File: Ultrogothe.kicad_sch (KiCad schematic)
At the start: 2 parts, among them J1 Conn_01x20, J2 Conn_01x20

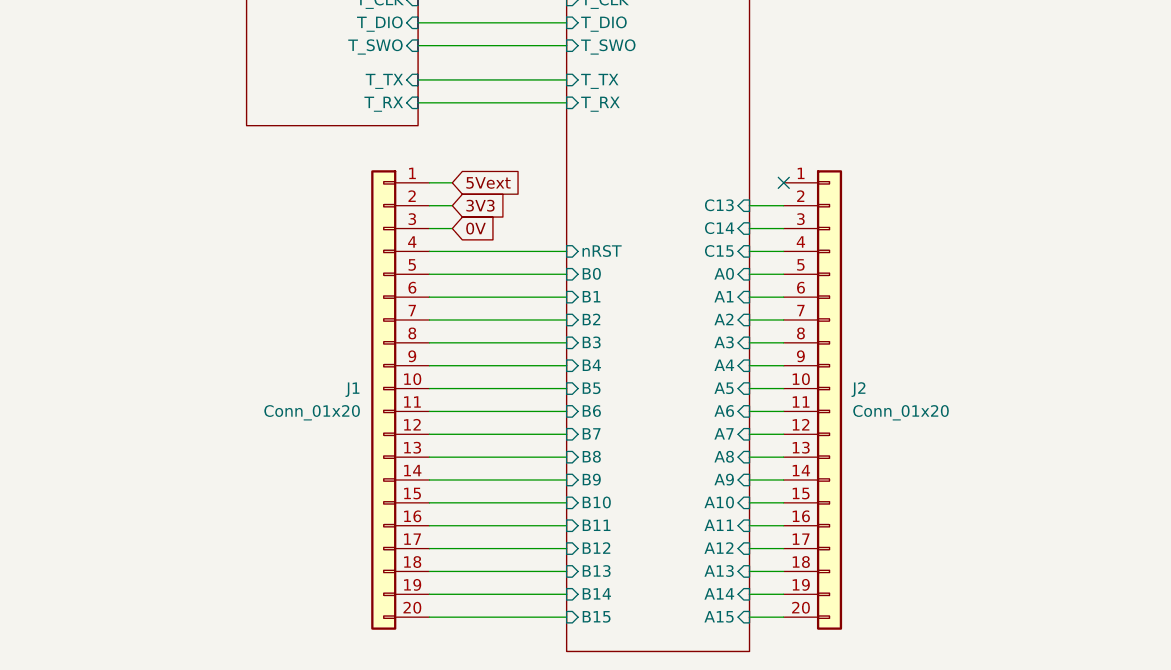
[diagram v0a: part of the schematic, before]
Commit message: répartition pins encours
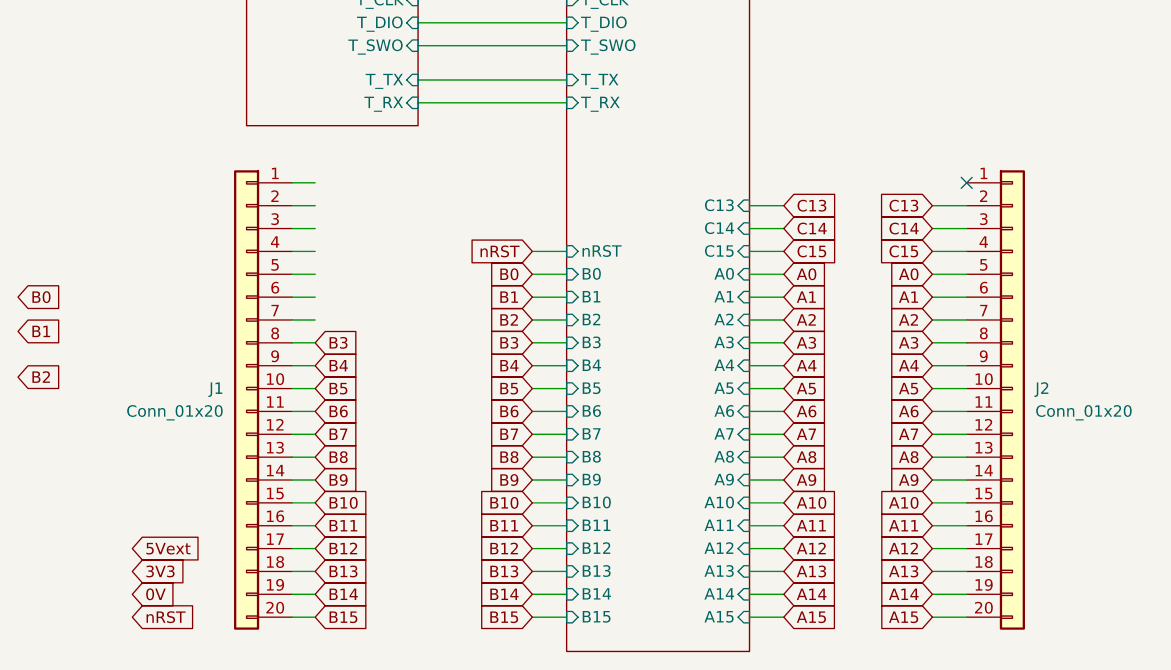
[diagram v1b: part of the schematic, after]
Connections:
- net 0V: no longer J1.3 (Pin_3)
- net 3V3: no longer J1.2 (Pin_2)
- net 5Vext: no longer J1.1 (Pin_1)
- net s_uC/A0 renamed A0
- net s_uC/A1 renamed A1
- net s_uC/A10 renamed A10
- net s_uC/A11 renamed A11
- net s_uC/A12 renamed A12
- net s_uC/A13 renamed A13
- net s_uC/A14 renamed A14
- net s_uC/A15 renamed A15
- net s_uC/A2 renamed A2
- net s_uC/A3 renamed A3
- net s_uC/A4 renamed A4
- net s_uC/A5 renamed A5
- net s_uC/A6 renamed A6
- net s_uC/A7 renamed A7
- net s_uC/A8 renamed A8
- net s_uC/A9 renamed A9
- net s_uC/B0: no longer names the net of J1.5 (Pin_5)
- net s_uC/B1: no longer names the net of J1.6 (Pin_6)
- net s_uC/B10 renamed B10
- net s_uC/B11 renamed B11
- net s_uC/B12 renamed B12
- net s_uC/B13 renamed B13
- net s_uC/B14 renamed B14
- net s_uC/B15 renamed B15
- net s_uC/B2: no longer names the net of J1.7 (Pin_7)
- net s_uC/B3 renamed B3
- net s_uC/B4 renamed B4
- net s_uC/B5 renamed B5
- net s_uC/B6 renamed B6
- net s_uC/B7 renamed B7
- net s_uC/B8 renamed B8
- net s_uC/B9 renamed B9
- net s_uC/C13 renamed C13
- net s_uC/C14 renamed C14
- net s_uC/C15 renamed C15
- net s_uC/nRST: no longer names the net of J1.4 (Pin_4)
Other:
- moved on the sheet: J1, J2

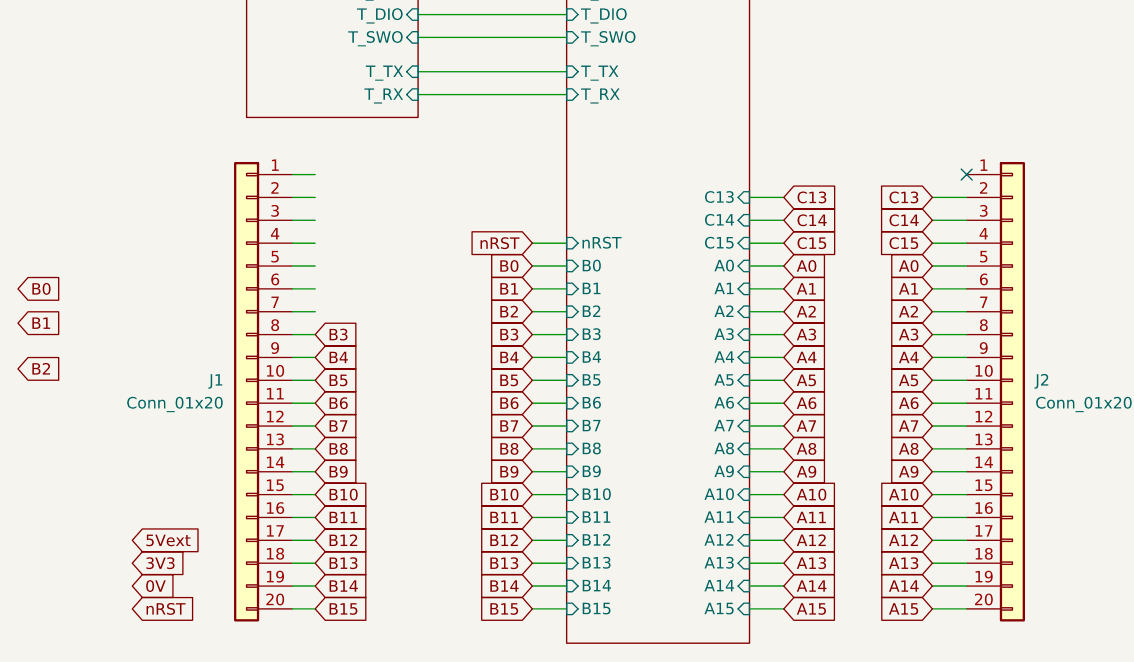
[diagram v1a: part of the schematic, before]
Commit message: répartition pins et routage
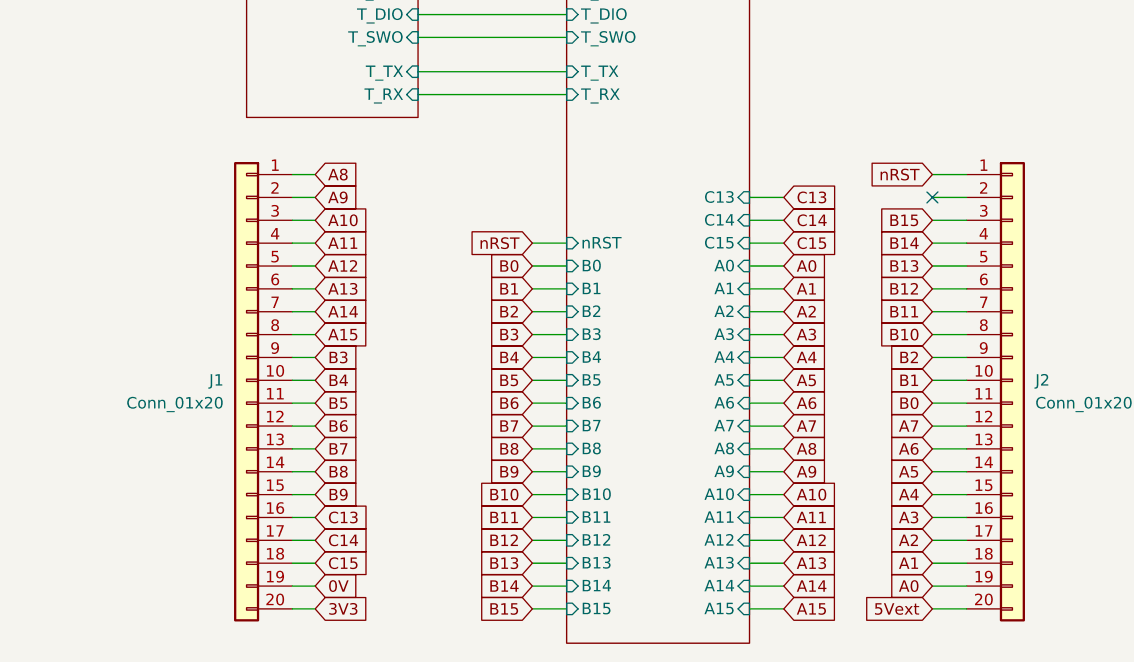
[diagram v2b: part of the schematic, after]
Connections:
- net 0V: now also J1.19 (Pin_19)
- net 3V3: now also J1.20 (Pin_20)
- net 5Vext: now also J2.20 (Pin_20)
- net A0: now also J2.19 (Pin_19); no longer J2.5 (Pin_5)
- net A1: now also J2.18 (Pin_18); no longer J2.6 (Pin_6)
- net A10: now also J1.3 (Pin_3); no longer J2.15 (Pin_15)
- net A11: now also J1.4 (Pin_4); no longer J2.16 (Pin_16)
- net A12: now also J1.5 (Pin_5); no longer J2.17 (Pin_17)
- net A13: now also J1.6 (Pin_6); no longer J2.18 (Pin_18)
- net A14: now also J1.7 (Pin_7); no longer J2.19 (Pin_19)
- net A15: now also J1.8 (Pin_8); no longer J2.20 (Pin_20)
- net A2: now also J2.17 (Pin_17); no longer J2.7 (Pin_7)
- net A3: now also J2.16 (Pin_16); no longer J2.8 (Pin_8)
- net A4: now also J2.15 (Pin_15); no longer J2.9 (Pin_9)
- net A5: now also J2.14 (Pin_14); no longer J2.10 (Pin_10)
- net A6: now also J2.13 (Pin_13); no longer J2.11 (Pin_11)
- net A8: now also J1.1 (Pin_1); no longer J2.13 (Pin_13)
- net A9: now also J1.2 (Pin_2); no longer J2.14 (Pin_14)
- net B0: now also J2.11 (Pin_11)
- net B1: now also J2.10 (Pin_10)
- net B10: now also J2.8 (Pin_8); no longer J1.15 (Pin_15)
- net B11: now also J2.7 (Pin_7); no longer J1.16 (Pin_16)
- net B12: now also J2.6 (Pin_6); no longer J1.17 (Pin_17)
- net B13: now also J2.5 (Pin_5); no longer J1.18 (Pin_18)
- net B14: now also J2.4 (Pin_4); no longer J1.19 (Pin_19)
- net B15: now also J2.3 (Pin_3); no longer J1.20 (Pin_20)
- net B2: now also J2.9 (Pin_9)
- net B3: now also J1.9 (Pin_9); no longer J1.8 (Pin_8)
- net B4: now also J1.10 (Pin_10); no longer J1.9 (Pin_9)
- net B5: now also J1.11 (Pin_11); no longer J1.10 (Pin_10)
- net B6: now also J1.12 (Pin_12); no longer J1.11 (Pin_11)
- net B7: now also J1.13 (Pin_13); no longer J1.12 (Pin_12)
- net B8: now also J1.14 (Pin_14); no longer J1.13 (Pin_13)
- net B9: now also J1.15 (Pin_15); no longer J1.14 (Pin_14)
- net C13: now also J1.16 (Pin_16); no longer J2.2 (Pin_2)
- net C14: now also J1.17 (Pin_17); no longer J2.3 (Pin_3)
- net C15: now also J1.18 (Pin_18); no longer J2.4 (Pin_4)
- net nRST: now also J2.1 (Pin_1)

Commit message: routage fini
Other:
- sheet s_debugger ports: added none; removed T_CLK, T_DIO, T_RST, T_RX, T_SWO, T_TX
- sheet s_uC ports: added none; removed T_CLK, T_DIO, T_RST, T_RX, T_SWO, T_TX
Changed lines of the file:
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@@
-    (stroke (width 0) (type default))
-  )
-  (wire (pts (xy 121.92 76.2) (xy 138.43 76.2))
-    (stroke (width 0) (type default))
-  )
-  (wire (pts (xy 121.92 73.66) (xy 138.43 73.66))
     (stroke (width 0) (type default))
   )
@@
     (stroke (width 0) (type default))
   )
-  (wire (pts (xy 121.92 71.12) (xy 138.43 71.12))
-    (stroke (width 0) (type default))
-  )
   (wire (pts (xy 134.62 99.06) (xy 138.43 99.06))
     (stroke (width 0) (type default))
@@
     (stroke (width 0) (type default))
   )
-  (wire (pts (xy 121.92 80.01) (xy 138.43 80.01))
-    (stroke (width 0) (type default))
-  )
   (wire (pts (xy 179.07 109.22) (xy 182.88 109.22))
     (stroke (width 0) (type default))
@@
     (stroke (width 0) (type default))
   )
-  (wire (pts (xy 121.92 68.58) (xy 138.43 68.58))
-    (stroke (width 0) (type default))
-  )
   (wire (pts (xy 179.07 104.14) (xy 182.88 104.14))
     (stroke (width 0) (type default))
@@
   )
   (wire (pts (xy 158.75 109.22) (xy 162.56 109.22))
-    (stroke (width 0) (type default))
-  )
-  (wire (pts (xy 121.92 82.55) (xy 138.43 82.55))
     (stroke (width 0) (type default))
   )
@@
     )
   )
-  (sheet (at 102.87 55.88) (size 19.05 29.21) (fields_autoplaced)
+  (sheet (at 102.87 55.88) (size 19.05 10.16) (fields_autoplaced)
     (stroke (width 0.1524) (type solid))
     (fill (color 0 0 0 0.0000))
@@
       (effects (font (size 1.27 1.27)) (justify left bottom))
     )
-    (property "Sheetfile" "s_debugger.kicad_sch" (at 102.87 85.6746 0)
+    (property "Sheetfile" "s_debugger.kicad_sch" (at 102.87 66.6246 0)
       (effects (font (size 1.27 1.27)) (justify left top) hide)
-    )
-    (pin "T_RX" input (at 121.92 82.55 0)
-      (effects (font (size 1.27 1.27)) (justify right))
-    )
-    (pin "T_TX" input (at 121.92 80.01 0)
-      (effects (font (size 1.27 1.27)) (justify right))
-    )
-    (pin "T_RST" input (at 121.92 68.58 0)
-      (effects (font (size 1.27 1.27)) (justify right))
-    )
-    (pin "T_CLK" input (at 121.92 71.12 0)
-      (effects (font (size 1.27 1.27)) (justify right))
-    )
-    (pin "T_SWO" input (at 121.92 76.2 0)
-      (effects (font (size 1.27 1.27)) (justify right))
-    )
-    (pin "T_DIO" input (at 121.92 73.66 0)
-      (effects (font (size 1.27 1.27)) (justify right))
     )
     (pin "0V" input (at 121.92 63.5 0)
@@
       (effects (font (size 1.27 1.27)) (justify left top) hide)
     )
-    (pin "T_TX" input (at 138.43 80.01 180)
-      (effects (font (size 1.27 1.27)) (justify left))
-    )
-    (pin "T_RX" input (at 138.43 82.55 180)
-      (effects (font (size 1.27 1.27)) (justify left))
-    )
-    (pin "T_CLK" input (at 138.43 71.12 180)
-      (effects (font (size 1.27 1.27)) (justify left))
-    )
-    (pin "T_RST" input (at 138.43 68.58 180)
-      (effects (font (size 1.27 1.27)) (justify left))
-    )
-    (pin "T_SWO" input (at 138.43 76.2 180)
-      (effects (font (size 1.27 1.27)) (justify left))
-    )
     (pin "0V" input (at 138.43 63.5 180)
       (effects (font (size 1.27 1.27)) (justify left))
@@
       (effects (font (size 1.27 1.27)) (justify left))
     )
-    (pin "T_DIO" input (at 138.43 73.66 180)
-      (effects (font (size 1.27 1.27)) (justify left))
-    )

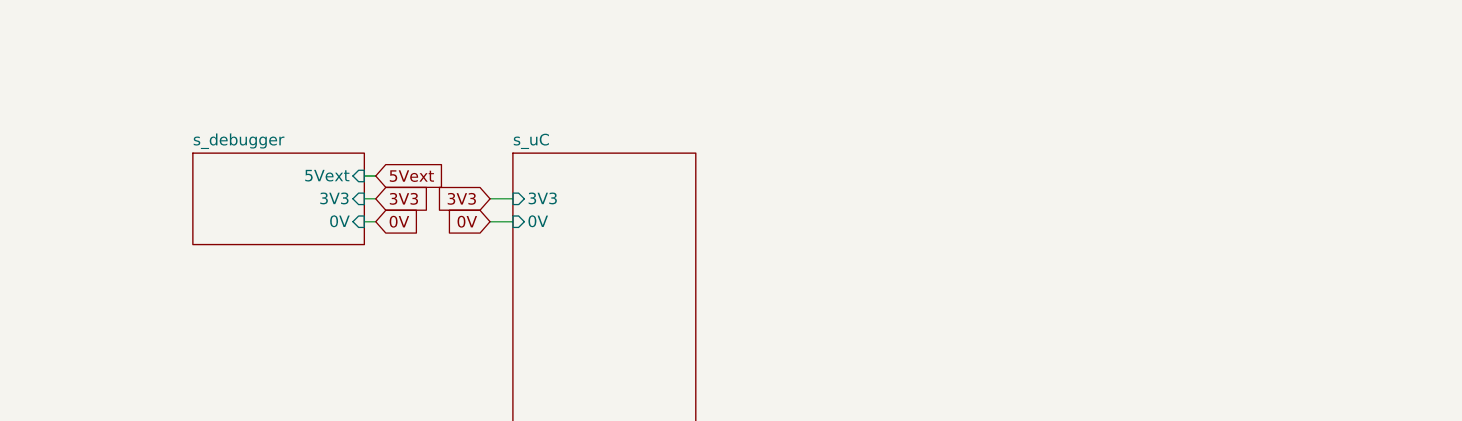
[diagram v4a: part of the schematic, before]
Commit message: Chgt connecteur programmation
passage à 2,54mm
alignement avec grille
silk: ajout pins
maj schéma pour clarification
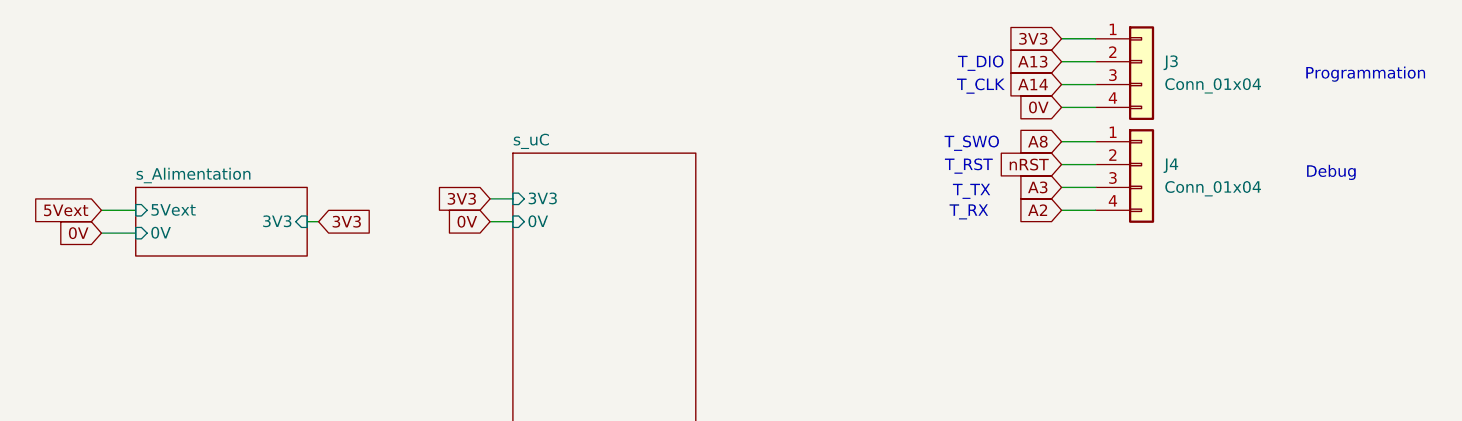
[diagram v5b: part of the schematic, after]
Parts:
- added J3, J4: Conn_01x04, Chimere_comps:PinHeader_1x04_P2.54mm_Simple, symbol Connector_Generic:Conn_01x04
- J1, J2: footprint Connector_PinHeader_2.54mm:PinHeader_1x20_P2.54mm_Vertical -> Chimere_comps:PinHeader_1x20_P2.54mm_Simple
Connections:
- net 0V: now also J3.4 (Pin_4)
- net 3V3: now also J3.1 (Pin_1)
- net A13: now also J3.2 (Pin_2)
- net A14: now also J3.3 (Pin_3)
- net A2: now also J4.4 (Pin_4)
- net A3: now also J4.3 (Pin_3)
- net A8: now also J4.1 (Pin_1)
- net nRST: now also J4.2 (Pin_2)
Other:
- sheet s_debugger renamed s_Alimentation
- sheet s_Alimentation: file s_debugger.kicad_sch -> s_Alimentation.kicad_sch
- note added: "Debug"
- note added: "Programmation"
- note added: "T_CLK"
- note added: "T_DIO"
- note added: "T_RST"
- note added: "T_RX"
- note added: "T_SWO"
- note added: "T_TX"

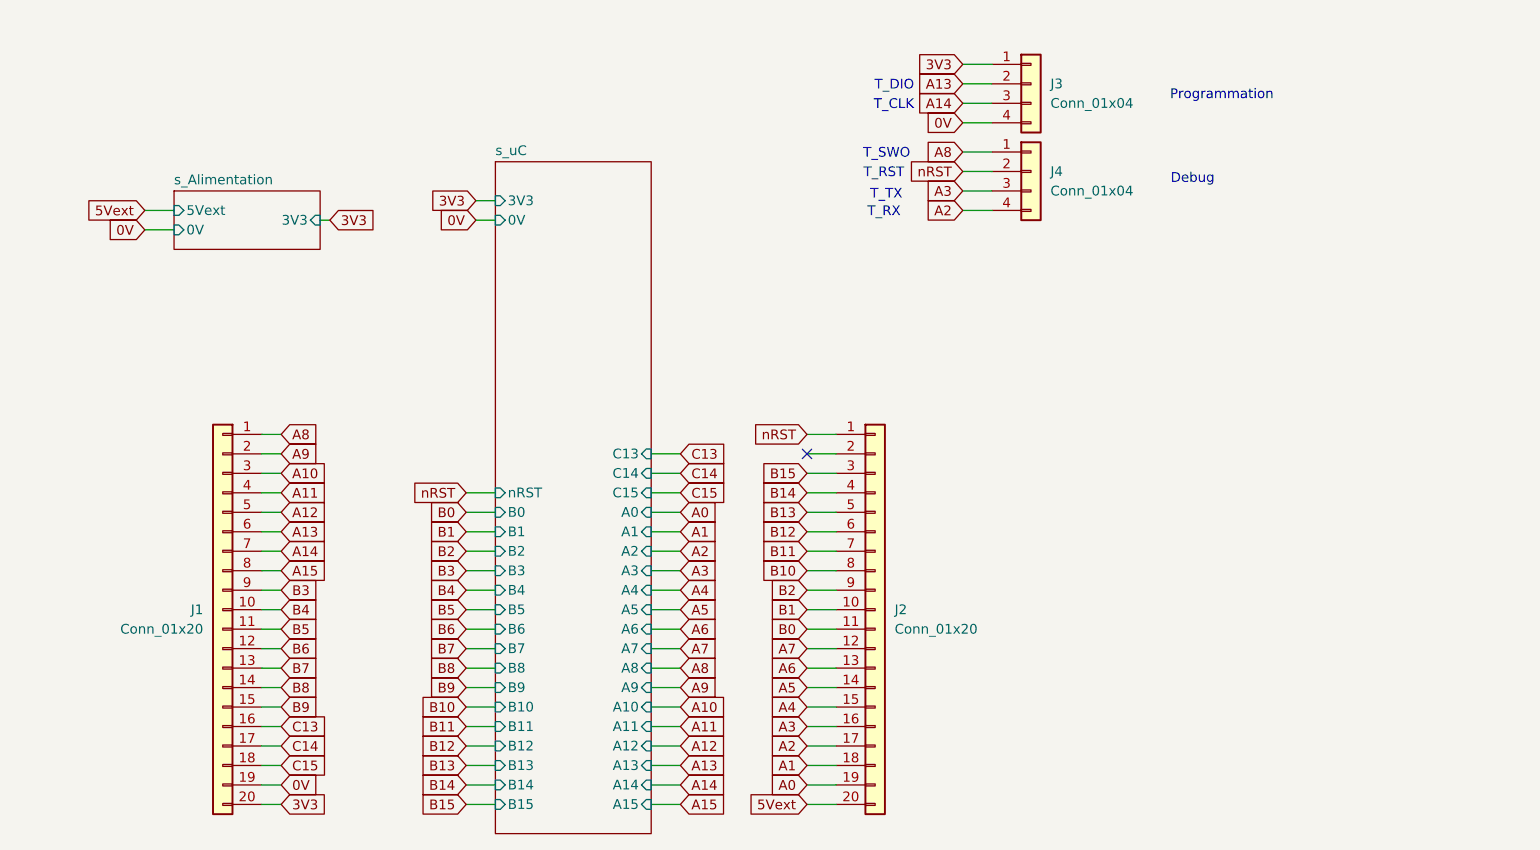
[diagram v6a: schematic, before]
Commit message: changement connecteur prog/debug par ST14
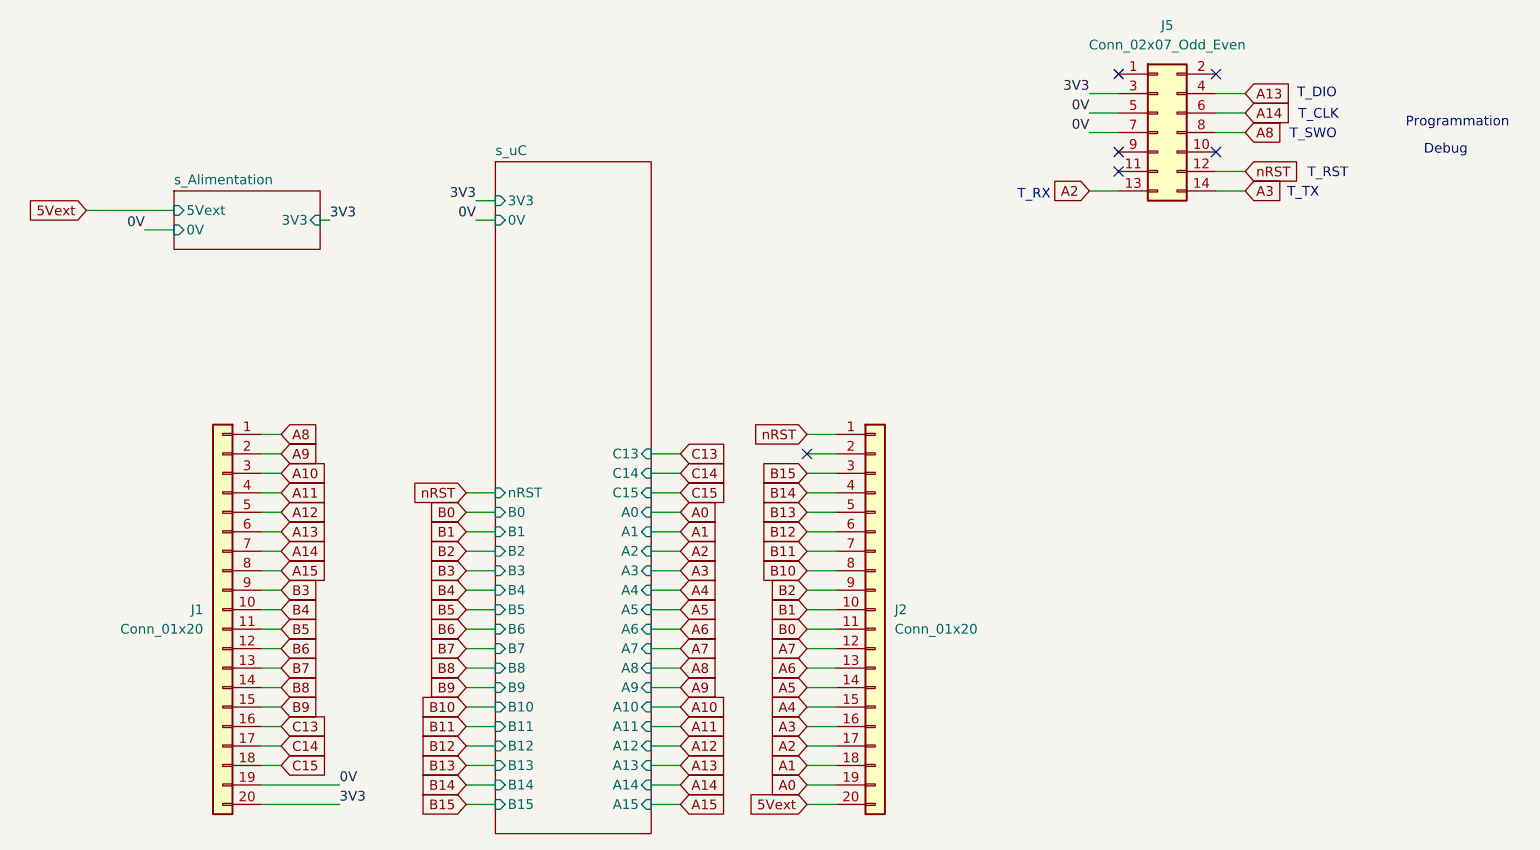
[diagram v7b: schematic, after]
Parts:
- removed J3, J4: Conn_01x04, Chimere_comps:PinHeader_1x04_P2.54mm_Simple, symbol Connector_Generic:Conn_01x04
- added J5: Conn_02x07_Odd_Even, Connector_PinHeader_1.27mm:PinHeader_2x07_P1.27mm_Vertical, symbol Connector_Generic:Conn_02x07_Odd_Even
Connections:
- net 0V: now also J5.5 (Pin_5), J5.7 (Pin_7)
- net 3V3: now also J5.3 (Pin_3)
- net A13: now also J5.4 (Pin_4)
- net A14: now also J5.6 (Pin_6)
- net A2: now also J5.13 (Pin_13)
- net A3: now also J5.14 (Pin_14)
- net A8: now also J5.8 (Pin_8)
- net nRST: now also J5.12 (Pin_12)
- no-connect marks 1 -> 6
